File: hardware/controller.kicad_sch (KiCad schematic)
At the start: 4 parts, among them J1 DevKitC-1 socket J1, J2 DevKitC-1 socket J3

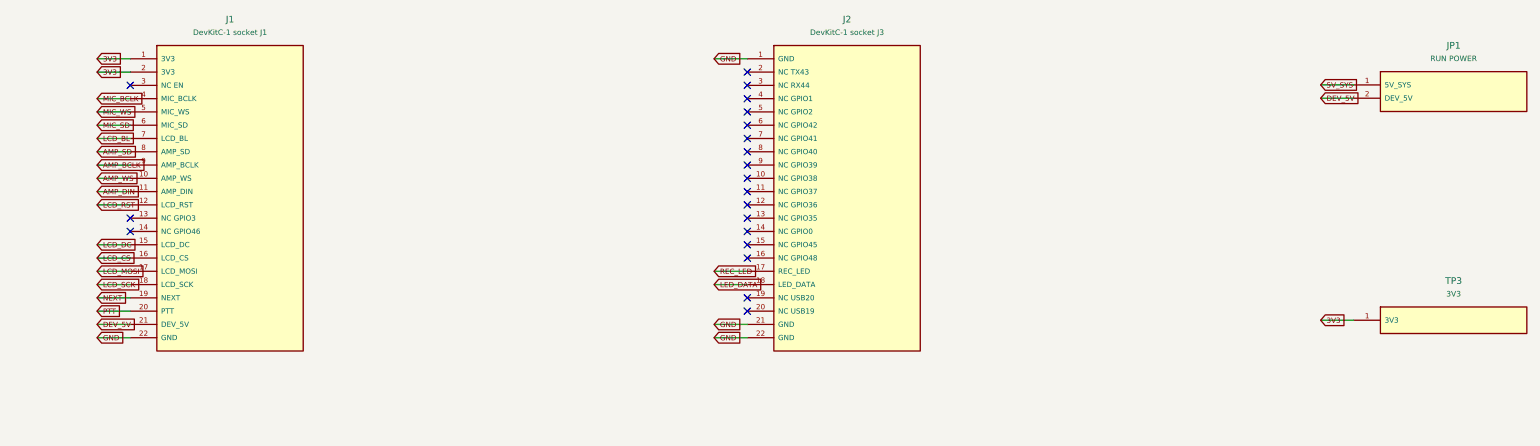
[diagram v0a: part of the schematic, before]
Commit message: engineering: Rev B zero-interference CAD, sealed STL meshes and carrier corrections
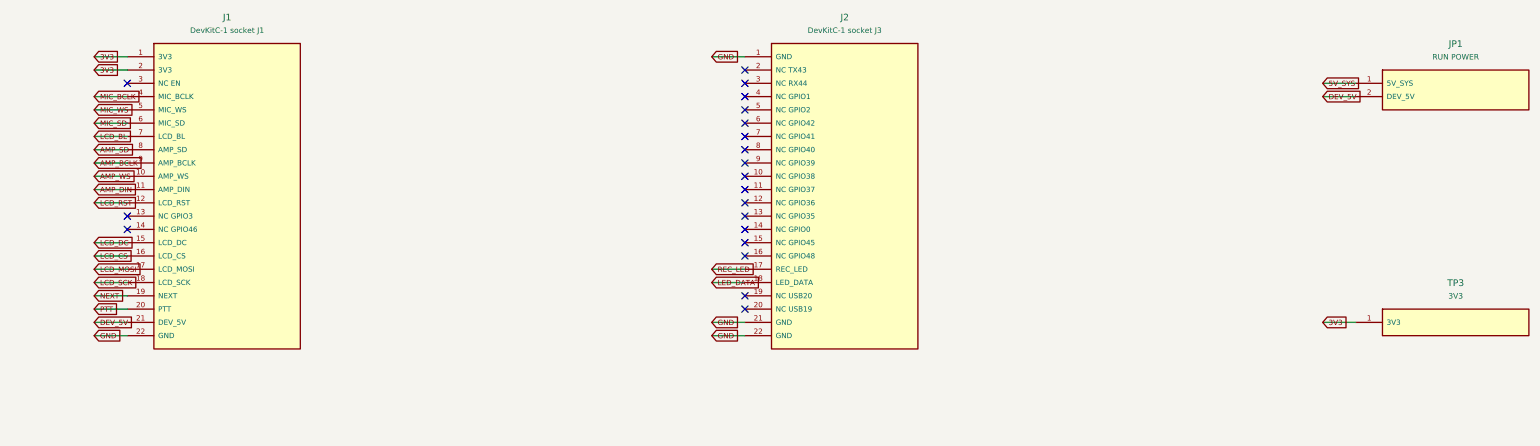
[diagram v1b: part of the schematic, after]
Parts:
- J1: footprint Aether:Socket_1x22_P2.54 -> Aether:Socket_1x22_P2.54_J1
- J2: footprint Aether:Socket_1x22_P2.54 -> Aether:Socket_1x22_P2.54_J2
- JP1: footprint Aether:PinHeader_1x02_P2.54 -> Aether:PinHeader_1x02_P2.54_JP1
- TP3: footprint Aether:TestPoint_THT_D2 -> Aether:TestPoint_THT_D2_TP3
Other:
- moved on the sheet: J1, J2, TP3
